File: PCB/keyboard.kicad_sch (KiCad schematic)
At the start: 118 parts, among them J101 USB4510-03-1-A, J103 CONN_DISPLAY, J2 AudioJack4, J4 switch, U2 USBLC6-2SC6, U3 USBLC6-2SC6, U4 RP2040, U5 W25Q128JVSIQ, Y1 12MHz

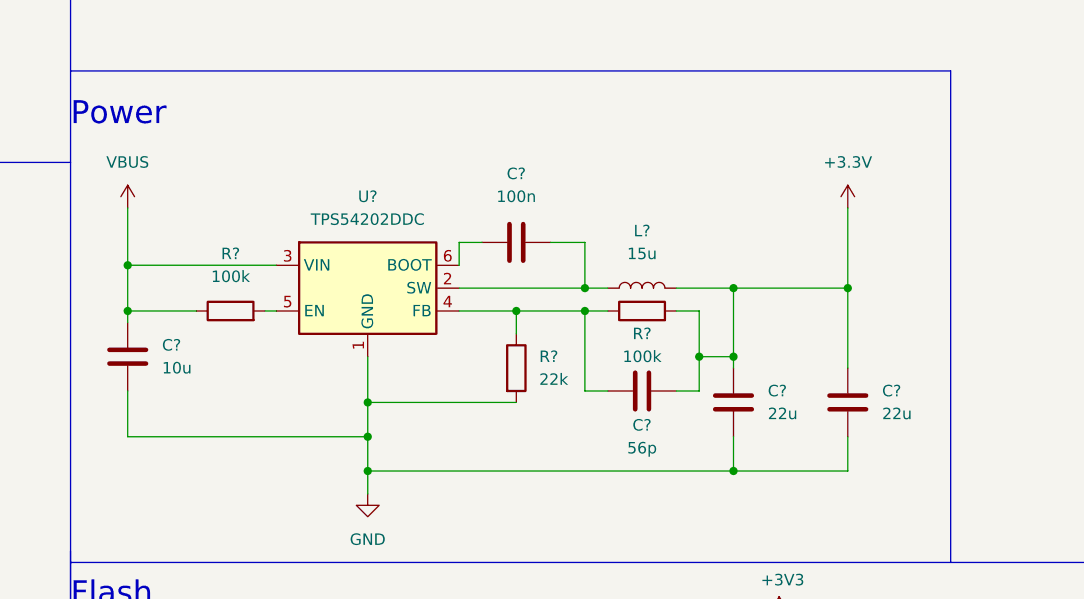
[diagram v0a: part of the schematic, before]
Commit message: Update footprint library
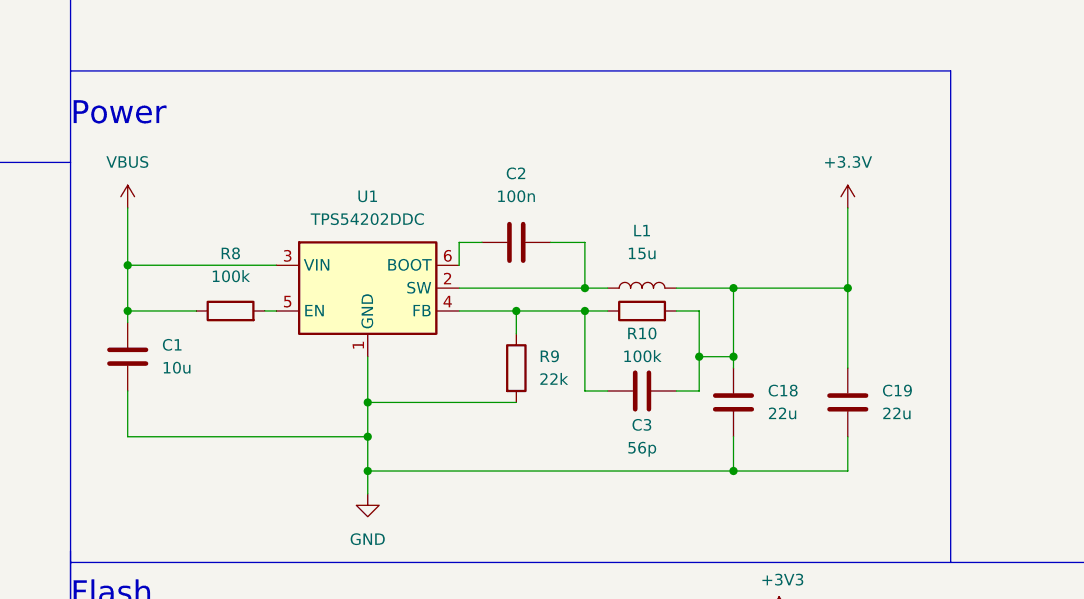
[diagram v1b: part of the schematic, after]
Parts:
- MX101, MX102, MX103, MX104, MX105, MX106, MX107, MX108, MX109, MX110, MX111, MX112, MX113, MX114, MX115, MX116, MX117, MX118, MX201, MX202, MX203, MX204, MX205, MX206, MX207, MX208, MX209, MX210, MX211, MX212, MX213, MX214, MX215, MX216, MX217, MX218: footprint SOFLE:CherryMX_KailhLowProfile_Hotswap -> Footprints:CherryMX_Choc_Hotswap
- gave numbers to parts that had none: 10

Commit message: wip full sch
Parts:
- removed U4: RP2040, RP2040:SC090813, symbol MCU_RaspberryPi_RP2040:RP2040
- added C201: 10u, symbol Device:C
- added C202: 100n, symbol Device:C
- added C203: 56p, symbol Device:C
- added C204, C205, C206, C207, C208, C209, C210, C211, C212, C215: 100n, Capacitor_SMD:C_0402_1005Metric, symbol Device:C
- added C213, C214: 1u, Capacitor_SMD:C_0402_1005Metric, symbol Device:C
- added C216, C217: 20p, Capacitor_SMD:C_0402_1005Metric, symbol Device:C
- added C218, C219: 22u, symbol Device:C
- added D221, D222: LED, symbol Device:LED
- added J201: USB4510-03-1-A, USB4510-03-1-A_GCT, symbol USB4510-03-1-A:USB4510-03-1-A
- added J202: AudioJack4, symbol Connector:AudioJack4
- added J203: CONN_DISPLAY, symbol Connector:Conn_01x04_Male
- added J204: switch, Connector_PinHeader_2.54mm:PinHeader_1x02_P2.54mm_Vertical, symbol Switch:SW_Push
- added L201: 15u, symbol Device:L
- added R201, R202: 5.1k, Resistor_SMD:R_0603_1608Metric, symbol Device:R
- added R203, R204: 27, Resistor_SMD:R_0402_1005Metric, symbol Device:R
- added R205: 10k, Resistor_SMD:R_0402_1005Metric, symbol Device:R
- added R206, R207: 1k, Resistor_SMD:R_0402_1005Metric, symbol Device:R
- added R208, R210: 100k, symbol Device:R
- added R209: 22k, symbol Device:R
- added R211, R212: 2.2K, Resistor_SMD:R_0402_1005Metric, symbol Device:R
- added R213, R214: 4.7K, Resistor_SMD:R_0402_1005Metric, symbol Device:R
- added U102, U103: USBLC6-2SC6, Package_TO_SOT_SMD:SOT-23-6, symbol Power_Protection:USBLC6-2SC6
- added U104, U204: RP2040, RP2040_minimal:RP2040-QFN-56, symbol Raspberry Pi:RP2040
- added U201: TPS54202DDC, Package_TO_SOT_SMD:SOT-23-6, symbol Regulator_Switching:TPS54202DDC
- added U205: W25Q128JVSIQ, Package_SO:SOIC-8_5.23x5.23mm_P1.27mm, symbol Memory_Flash:W25Q128JVS
- added Y201: 12MHz, Oscillator:Oscillator_SMD_Abracon_ASE-4Pin_3.2x2.5mm, symbol Device:Crystal_GND24
- J101: footprint USB4510-03-1-A:USB4510-03-1-A -> USB4510-03-1-A_GCT
- renumbered C1 to C101, C2 to C102, C3 to C103, C4 to C104, C5 to C105, C6 to C106, C7 to C107, C8 to C108, C9 to C109, C10 to C110, C11 to C111, C12 to C112, C13 to C113, C14 to C114, C15 to C115, C16 to C116, C17 to C117, C18 to C118, C19 to C119, DD103 to D103, D21 to D121, D22 to D122, J2 to J102, J4 to J104, L1 to L101, R1 to R101, R2 to R102, R3 to R103, R4 to R104, R5 to R105, R6 to R106, R7 to R107, R8 to R108, R9 to R109, R10 to R110, R13 to R111, R12 to R112, R108 to R113, R109 to R114, U1 to U101, U5 to U105, U2 to U202, U3 to U203, Y1 to Y101
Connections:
- net USB__CONN_D+ is gone; now on net USB_CONN_D+: J101.A6 (DP1), U202.1 (I/O1)
- net USB__CONN_D- is gone; now on net USB_CONN_D-: J101.A7 (DN1)
- net +1V1: now also C204.1, C205.1, C213.1, U104.23 (DVDD), U104.45 (VREG_VOUT), U104.50 (DVDD), U204.23 (DVDD), U204.45 (VREG_VOUT), U204.50 (DVDD)
- net +3.3V: now also C203.1, C218.1, C219.1, J203.2 (Pin_2), L201.2, R210.2, Y201.4
- net +3V3: now also C206.1, C207.1, C208.1, C209.1, C210.1, C211.1, C212.1, C214.1, C215.1, D222.2 (A), J202.S, R205.1, R213.2, R214.2, U103.5 (VBUS), U104.1 (IOVDD), U104.10 (IOVDD), U104.22 (IOVDD), U104.33 (IOVDD), U104.42 (IOVDD), U104.43 (ADC_AVDD), U104.44 (VREG_IN), U104.48 (USB_VDD), U104.49 (IOVDD), U204.1 (IOVDD), U204.10 (IOVDD), U204.22 (IOVDD), U204.33 (IOVDD), U204.42 (IOVDD), U204.43 (ADC_AVDD), U204.44 (VREG_IN), U204.48 (USB_VDD), U204.49 (IOVDD), U205.8 (VCC)
- net CC1: now also J201.A5 (CC1), R201.2
- net CC2: now also J201.B5 (CC2), R202.2
- net GND: now also J101.B4-A9 (VBUS), C201.2, C204.2, C205.2, C206.2, C207.2, C208.2, C209.2, C210.2, C211.2, C212.2, C213.2, C214.2, C215.2, C216.2, C217.2, C218.2, C219.2, J201.A1-B12 (GND), J201.B4-A9 (VBUS), J202.T, J203.1 (Pin_1), J204.2, R201.1, R202.1, R209.2, R211.1, R212.1, U102.2 (GND), U103.2 (GND), U104.19 (TESTEN), U104.57 (GND), U201.1 (GND), U204.19 (TESTEN), U204.57 (GND), U205.4 (GND), Y201.2; no longer J101.B1-A12 (GND)
- net GPIO26_ADC0: now also U204.38 (GPIO26_ADC0)
- net GPIO27_ADC1: now also U204.39 (GPIO27_ADC1)
- net GPIO28_ADC2: now also U204.40 (GPIO28_ADC2)
- net GPIO29_ADC3: now also U204.41 (GPIO29_ADC3)
- net L-COL-1: now also MX101.1, MX102.1, MX103.1, U104.7 (GPIO5); no longer MX201.1, MX202.1, MX203.1
- net L-COL-2: now also MX104.1, MX105.1, MX106.1, U104.8 (GPIO6); no longer MX204.1, MX205.1, MX206.1
- net L-COL-3: now also MX107.1, MX108.1, MX109.1, U104.9 (GPIO7); no longer MX207.1, MX208.1, MX209.1
- net L-COL-4: now also MX110.1, MX111.1, MX112.1, U104.11 (GPIO8); no longer MX210.1, MX211.1, MX212.1
- net L-COL-5: now also MX113.1, MX114.1, MX115.1, U104.12 (GPIO9); no longer MX213.1, MX214.1, MX215.1
- net L-COL-6: now also MX116.1, MX117.1, MX118.1, U104.13 (GPIO10); no longer MX216.1, MX217.1, MX218.1
- net L-ROW-1: now also D101.1 (K), D104.1 (K), D107.1 (K), D110.1 (K), D113.1 (K), D116.1 (K), U104.4 (GPIO2); no longer D201.1 (K), D204.1 (K), D207.1 (K), D210.1 (K), D213.1 (K), D216.1 (K)
- net L-ROW-2: now also D102.1 (K), D105.1 (K), D108.1 (K), D111.1 (K), D114.1 (K), D117.1 (K), U104.5 (GPIO3); no longer D202.1 (K), D205.1 (K), D208.1 (K), D211.1 (K), D214.1 (K), D217.1 (K)
- net L-ROW-3: now also D103.1 (K), D106.1 (K), D109.1 (K), D112.1 (K), D115.1 (K), D118.1 (K), U104.6 (GPIO4); no longer D203.1 (K), D206.1 (K), D209.1 (K), D212.1 (K), D215.1 (K), D218.1 (K)
- net LED: now also D221.2 (A), U204.37 (GPIO25); no longer D121.2 (A)
- net QSPI_SCLK: now also U204.52 (QSPI_SCLK), U205.6 (CLK)
- net QSPI_SD0: now also U204.53 (QSPI_SD0), U205.5 (DI(IO0))
- net QSPI_SD1: now also U204.55 (QSPI_SD1), U205.2 (DO(IO1))
- net QSPI_SD2: now also U204.54 (QSPI_SD2), U205.3 (IO2)
- net QSPI_SD3: now also U204.51 (QSPI_SD3), U205.7 (IO3)
- net QSPI_SS: now also R205.2, R206.1, U204.56 (QSPI_SS), U205.1 (~{CS})
- net R-COL-1: now also MX201.1, MX202.1, MX203.1, U204.7 (GPIO5); no longer MX101.1, MX102.1, MX103.1
- net R-COL-2: now also MX204.1, MX205.1, MX206.1, U204.8 (GPIO6); no longer MX104.1, MX105.1, MX106.1
- net R-COL-3: now also MX207.1, MX208.1, MX209.1, U204.9 (GPIO7); no longer MX107.1, MX108.1, MX109.1
- net R-COL-4: now also MX210.1, MX211.1, MX212.1, U204.11 (GPIO8); no longer MX110.1, MX111.1, MX112.1
- net R-COL-5: now also MX213.1, MX214.1, MX215.1, U204.12 (GPIO9); no longer MX113.1, MX114.1, MX115.1
- net R-COL-6: now also MX216.1, MX217.1, MX218.1, U204.13 (GPIO10); no longer MX116.1, MX117.1, MX118.1
- net R-ROW-1: now also D201.1 (K), D204.1 (K), D207.1 (K), D210.1 (K), D213.1 (K), D216.1 (K), U204.4 (GPIO2); no longer D101.1 (K), D104.1 (K), D107.1 (K), D110.1 (K), D113.1 (K), D116.1 (K)
- net R-ROW-2: now also D202.1 (K), D205.1 (K), D208.1 (K), D211.1 (K), D214.1 (K), D217.1 (K), U204.5 (GPIO3); no longer D102.1 (K), D105.1 (K), D108.1 (K), D111.1 (K), D114.1 (K), D117.1 (K)
- net R-ROW-3: now also D203.1 (K), D206.1 (K), D209.1 (K), D212.1 (K), D215.1 (K), D218.1 (K), U204.6 (GPIO4); no longer D103.1 (K), D106.1 (K), D109.1 (K), D112.1 (K), D115.1 (K), D118.1 (K)
- net RUN: now also U204.26 (RUN)
- net RX_SPLIT: now also U103.6 (I/O1), U204.3 (GPIO1)
- net RX_SPLIT_CONN: now also J202.R2, U103.1 (I/O1)
- net SCL_DISPLAY: now also J203.3 (Pin_3), R214.1, U204.18 (GPIO15)
- net SDA_DISPLAY: now also J203.4 (Pin_4), R213.1, U204.17 (GPIO14)
- net SWCLK: now also U204.24 (SWCLK)
- net SWD: now also U204.25 (SWD)
- net TX_SPLIT: now also U103.4 (I/O2), U204.2 (GPIO0)
- net TX_SPLIT_CONN: now also J202.R1, U103.3 (I/O2)
- net USB_CONN_D+: now also J201.A6 (DP1), J201.B6 (DP2), U102.1 (I/O1)
- net USB_CONN_D-: now also J201.A7 (DN1), J201.B7 (DN2), U102.3 (I/O2)
- net USB_D+: now also R203.1, U102.6 (I/O1)
- net USB_D-: now also R204.1, U102.4 (I/O2)
- net VBUS: now also J101.B1-A12 (GND), C201.1, J201.A4-B9 (VBUS), J201.B1-A12 (GND), R208.1, U102.5 (VBUS), U201.3 (VIN); no longer J101.B4-A9 (VBUS)
- net XIN: now also C216.1, U204.20 (XIN), Y201.1
- net XOUT: now also R207.1, U204.21 (XOUT)
- net at R104.2: now also U104.46 (USB_DM)
- net at R103.2: now also U104.47 (USB_DP)
- net ~{USB_BOOT} renamed ~{L_BOOT}
- new net: C202.1, U201.6 (BOOT)
- new net: C202.2, L201.1, U201.2 (SW)
- new net: C217.1, R207.2, Y201.3
- new net: R208.2, U201.5 (EN)
- new net: C203.2, R209.1, R210.1, U201.4 (FB)
- new net: D222.1 (K), R211.2
- new net: R204.2, U204.46 (USB_DM)
- new net: R203.2, U204.47 (USB_DP)
- new net: D221.1 (K), R212.2
- new net L_LED: D121.2 (A), U104.37 (GPIO25)
- new net L_QSPI_SCLK: U104.52 (QSPI_SCLK)
- new net L_QSPI_SD0: U104.53 (QSPI_SD0)
- new net L_QSPI_SD1: U104.55 (QSPI_SD1)
- new net L_QSPI_SD2: U104.54 (QSPI_SD2)
- new net L_QSPI_SD3: U104.51 (QSPI_SD3)
- new net L_QSPI_SS: U104.56 (QSPI_SS)
- new net L_RUN: U104.26 (RUN)
- new net L_RX_SPLIT: U104.3 (GPIO1)
- new net L_SCL_DISPLAY: U104.18 (GPIO15)
- new net L_SDA_DISPLAY: U104.17 (GPIO14)
- new net L_SWCLK: U104.24 (SWCLK)
- new net L_SWD: U104.25 (SWD)
- new net L_TX_SPLIT: U104.2 (GPIO0)
- new net L_XIN: U104.20 (XIN)
- new net L_XOUT: U104.21 (XOUT)
- new net ~{R_BOOT}: J204.1, R206.2
- no-connect marks 14 -> 32
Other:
- added sheet USB Input (usb_input.kicad_sch)
- note added: "Left Flash"
- note added: "Left MCU"
- note added: "Left Power"
- note added: "Right Flash"
- note added: "Right MCU"
- note added: "Right Matrix"
- note added: "Right Power"
- note removed: "Flash"
- note removed: "MCU"
- note removed: "Power"
- note removed: "Right matrix"
- moved on the sheet: C101, C102, C103, C104, C105, C106, C107, C108, C109, C110, C111, C112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

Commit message: Layout done
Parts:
- removed C101, C201: 10u, symbol Device:C
- removed C102, C202: 100n, symbol Device:C
- removed C103, C203: 56p, symbol Device:C
- removed C104, C105, C106, C107, C108, C109, C110, C111, C112, C115, C204, C205, C206, C207, C208, C209, C210, C211, C212, C215: 100n, Capacitor_SMD:C_0402_1005Metric, symbol Device:C
- removed C113, C114, C213, C214: 1u, Capacitor_SMD:C_0402_1005Metric, symbol Device:C
- removed C116, C117, C216, C217: 20p, Capacitor_SMD:C_0402_1005Metric, symbol Device:C
- removed C118, C119, C218, C219: 22u, symbol Device:C
- removed D101, D102, D103, D104, D105, D106, D107, D108, D109, D110, D111, D112, D113, D114, D115, D116, D117, D118, D201, D202, D203, D204, D205, D206, D207, D208, D209, D210, D211, D212, D213, D214, D215, D216, D217, D218: DIODE, Diode_SMD:D_SOD-123, symbol Diode:1N4148W
- removed D121, D122, D221, D222: LED, symbol Device:LED
- removed J101, J201: USB4510-03-1-A, USB4510-03-1-A_GCT, symbol USB4510-03-1-A:USB4510-03-1-A
- removed J102, J202: AudioJack4, symbol Connector:AudioJack4
- removed J103, J203: CONN_DISPLAY, symbol Connector:Conn_01x04_Male
- removed J104, J204: switch, Connector_PinHeader_2.54mm:PinHeader_1x02_P2.54mm_Vertical, symbol Switch:SW_Push
- removed L101, L201: 15u, symbol Device:L
- removed MX101, MX102, MX103, MX104, MX105, MX106, MX107, MX108, MX109, MX110, MX111, MX112, MX113, MX114, MX115, MX116, MX117, MX118, MX201, MX202, MX203, MX204, MX205, MX206, MX207, MX208, MX209, MX210, MX211, MX212, MX213, MX214, MX215, MX216, MX217, MX218: SW_Push, Footprints:CherryMX_Choc_Hotswap, symbol Switch:SW_Push
- removed R101, R102, R201, R202: 5.1k, Resistor_SMD:R_0603_1608Metric, symbol Device:R
- removed R103, R104, R203, R204: 27, Resistor_SMD:R_0402_1005Metric, symbol Device:R
- removed R105, R205: 10k, Resistor_SMD:R_0402_1005Metric, symbol Device:R
- removed R106, R107, R206, R207: 1k, Resistor_SMD:R_0402_1005Metric, symbol Device:R
- removed R108, R110, R208, R210: 100k, symbol Device:R
- removed R109, R209: 22k, symbol Device:R
- removed R111, R112, R211, R212: 2.2K, Resistor_SMD:R_0402_1005Metric, symbol Device:R
- removed R113, R114, R213, R214: 4.7K, Resistor_SMD:R_0402_1005Metric, symbol Device:R
- removed U101, U201: TPS54202DDC, Package_TO_SOT_SMD:SOT-23-6, symbol Regulator_Switching:TPS54202DDC
- removed U102, U103, U202, U203: USBLC6-2SC6, Package_TO_SOT_SMD:SOT-23-6, symbol Power_Protection:USBLC6-2SC6
- removed U104, U204: RP2040, RP2040_minimal:RP2040-QFN-56, symbol Raspberry Pi:RP2040
- removed U105, U205: W25Q128JVSIQ, Package_SO:SOIC-8_5.23x5.23mm_P1.27mm, symbol Memory_Flash:W25Q128JVS
- removed Y101, Y201: 12MHz, Oscillator:Oscillator_SMD_Abracon_ASE-4Pin_3.2x2.5mm, symbol Device:Crystal_GND24
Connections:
- no-connect marks 32 -> 0
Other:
- removed sheet USB Input
- added sheet Left MCU (mcu.kicad_sch)
- added sheet Left Matix (key_matrix.kicad_sch)
- added sheet Right MCU (mcu.kicad_sch)
- added sheet Right Matrix (key_matrix.kicad_sch)
- added sheet TRRS Connection (trrs_conn.kicad_sch)
- note removed: "Connectors"
- note removed: "Crystal"
- note removed: "ESD Protection"
- note removed: "LEDs"
- note removed: "Left Flash"
- note removed: "Left MCU"
- note removed: "Left Matrix"
- note removed: "Left Power"
- note removed: "Make sure C13 is close to pin 45 of RP2040"
- note removed: "Make sure C14 is close to pin 44 of RP2040"
- note removed: "Make sure R3 and R4 are close to RP2040"
- note removed: "Make sure U2 is close to J1"
- note removed: "Right Flash"
- note removed: "Right MCU"
- note removed: "Right Matrix"
- note removed: "Right Power"
- note removed: "Route right half TX to left half RX Route left half TX to right half RX"
- note removed: "Thumb keys"
- title: (none) -> 36

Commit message: Work
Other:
- sheet Left MCU ports: added ROW-4; removed COL-6
- sheet Left Matix ports: added ROW-4; removed COL-6
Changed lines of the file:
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@@
     (rev "1.0")
   )
+  (wire (pts (xy 68.58 62.23) (xy 72.39 62.23))
+    (stroke (width 0) (type default) (color 0 0 0 0))
+  )
+  (wire (pts (xy 133.35 48.26) (xy 137.16 48.26))
+    (stroke (width 0) (type default) (color 0 0 0 0))
+  )
+  (wire (pts (xy 133.35 53.34) (xy 137.16 53.34))
+    (stroke (width 0) (type default) (color 0 0 0 0))
+  )
+  (wire (pts (xy 133.35 50.8) (xy 137.16 50.8))
+    (stroke (width 0) (type default) (color 0 0 0 0))
+  )
+  (wire (pts (xy 133.35 58.42) (xy 137.16 58.42))
+    (stroke (width 0) (type default) (color 0 0 0 0))
+  )
+  (wire (pts (xy 133.35 64.77) (xy 137.16 64.77))
+    (stroke (width 0) (type default) (color 0 0 0 0))
+  )
+  (wire (pts (xy 68.58 55.88) (xy 72.39 55.88))
+    (stroke (width 0) (type default) (color 0 0 0 0))
+  )
+  (wire (pts (xy 133.35 69.85) (xy 137.16 69.85))
+    (stroke (width 0) (type default) (color 0 0 0 0))
+  )
+  (wire (pts (xy 92.71 72.39) (xy 95.25 72.39))
+    (stroke (width 0) (type default) (color 0 0 0 0))
+  )
+  (wire (pts (xy 133.35 67.31) (xy 137.16 67.31))
+    (stroke (width 0) (type default) (color 0 0 0 0))
+  )
+  (wire (pts (xy 68.58 69.85) (xy 72.39 69.85))
+    (stroke (width 0) (type default) (color 0 0 0 0))
+  )
+  (wire (pts (xy 133.35 55.88) (xy 137.16 55.88))
+    (stroke (width 0) (type default) (color 0 0 0 0))
+  )
+  (wire (pts (xy 92.71 69.85) (xy 95.25 69.85))
+    (stroke (width 0) (type default) (color 0 0 0 0))
+  )
+  (wire (pts (xy 68.58 67.31) (xy 72.39 67.31))
+    (stroke (width 0) (type default) (color 0 0 0 0))
+  )
+  (wire (pts (xy 133.35 60.96) (xy 137.16 60.96))
+    (stroke (width 0) (type default) (color 0 0 0 0))
+  )
+  (wire (pts (xy 111.76 72.39) (xy 114.3 72.39))
+    (stroke (width 0) (type default) (color 0 0 0 0))
+  )
+  (polyline (pts (xy 299.72 165.1) (xy 299.72 165.1))
+    (stroke (width 0) (type default) (color 0 0 0 0))
+  )
+  (wire (pts (xy 68.58 53.34) (xy 72.39 53.34))
+    (stroke (width 0) (type default) (color 0 0 0 0))
+  )
+  (wire (pts (xy 68.58 48.26) (xy 72.39 48.26))
+    (stroke (width 0) (type default) (color 0 0 0 0))
+  )
+  (wire (pts (xy 111.76 69.85) (xy 114.3 69.85))
+    (stroke (width 0) (type default) (color 0 0 0 0))
+  )
+  (wire (pts (xy 68.58 50.8) (xy 72.39 50.8))
+    (stroke (width 0) (type default) (color 0 0 0 0))
+  )
   (wire (pts (xy 68.58 64.77) (xy 72.39 64.77))
     (stroke (width 0) (type default) (color 0 0 0 0))
   )
-  (wire (pts (xy 133.35 48.26) (xy 137.16 48.26))
-    (stroke (width 0) (type default) (color 0 0 0 0))
-  )
-  (wire (pts (xy 133.35 53.34) (xy 137.16 53.34))
-    (stroke (width 0) (type default) (color 0 0 0 0))
-  )
-  (wire (pts (xy 133.35 50.8) (xy 137.16 50.8))
-    (stroke (width 0) (type default) (color 0 0 0 0))
-  )
-  (wire (pts (xy 133.35 58.42) (xy 137.16 58.42))
-    (stroke (width 0) (type default) (color 0 0 0 0))
-  )
-  (wire (pts (xy 133.35 64.77) (xy 137.16 64.77))
-    (stroke (width 0) (type default) (color 0 0 0 0))
-  )
-  (wire (pts (xy 68.58 55.88) (xy 72.39 55.88))
-    (stroke (width 0) (type default) (color 0 0 0 0))
-  )
-  (wire (pts (xy 133.35 69.85) (xy 137.16 69.85))
-    (stroke (width 0) (type default) (color 0 0 0 0))
-  )
-  (wire (pts (xy 92.71 72.39) (xy 95.25 72.39))
-    (stroke (width 0) (type default) (color 0 0 0 0))
-  )
-  (wire (pts (xy 133.35 67.31) (xy 137.16 67.31))
-    (stroke (width 0) (type default) (color 0 0 0 0))
-  )
-  (wire (pts (xy 133.35 55.88) (xy 137.16 55.88))
-    (stroke (width 0) (type default) (color 0 0 0 0))
-  )
-  (wire (pts (xy 92.71 69.85) (xy 95.25 69.85))
-    (stroke (width 0) (type default) (color 0 0 0 0))
-  )
-  (wire (pts (xy 68.58 69.85) (xy 72.39 69.85))
-    (stroke (width 0) (type default) (color 0 0 0 0))
-  )
-  (wire (pts (xy 68.58 60.96) (xy 72.39 60.96))
-    (stroke (width 0) (type default) (color 0 0 0 0))
-  )
-  (wire (pts (xy 133.35 60.96) (xy 137.16 60.96))
-    (stroke (width 0) (type default) (color 0 0 0 0))
-  )
-  (wire (pts (xy 111.76 72.39) (xy 114.3 72.39))
-    (stroke (width 0) (type default) (color 0 0 0 0))
-  )
-  (polyline (pts (xy 299.72 165.1) (xy 299.72 165.1))
-    (stroke (width 0) (type default) (color 0 0 0 0))
-  )
-  (wire (pts (xy 68.58 53.34) (xy 72.39 53.34))
-    (stroke (width 0) (type default) (color 0 0 0 0))
-  )
-  (wire (pts (xy 68.58 48.26) (xy 72.39 48.26))
-    (stroke (width 0) (type default) (color 0 0 0 0))
-  )
-  (wire (pts (xy 111.76 69.85) (xy 114.3 69.85))
-    (stroke (width 0) (type default) (color 0 0 0 0))
-  )
-  (wire (pts (xy 68.58 50.8) (xy 72.39 50.8))
-    (stroke (width 0) (type default) (color 0 0 0 0))
-  )
-  (wire (pts (xy 68.58 67.31) (xy 72.39 67.31))
-    (stroke (width 0) (type default) (color 0 0 0 0))
-  )
   (wire (pts (xy 68.58 58.42) (xy 72.39 58.42))
     (stroke (width 0) (type default) (color 0 0 0 0))
@@
       (effects (font (size 1.27 1.27)) (justify left top) hide)
     )
-    (pin "ROW-2" input (at 68.58 67.31 0)
-      (effects (font (size 1.27 1.27)) (justify right))
-    )
-    (pin "ROW-3" input (at 68.58 69.85 0)
-      (effects (font (size 1.27 1.27)) (justify right))
-    )
-    (pin "ROW-1" input (at 68.58 64.77 0)
+    (pin "ROW-2" input (at 68.58 64.77 0)
+      (effects (font (size 1.27 1.27)) (justify right))
+    )
+    (pin "ROW-3" input (at 68.58 67.31 0)
+      (effects (font (size 1.27 1.27)) (justify right))
+    )
+    (pin "ROW-1" input (at 68.58 62.23 0)
       (effects (font (size 1.27 1.27)) (justify right))
     )
@@
       (effects (font (size 1.27 1.27)) (justify right))
     )
-    (pin "COL-6" input (at 68.58 60.96 0)
+    (pin "ROW-4" input (at 68.58 69.85 0)
       (effects (font (size 1.27 1.27)) (justify right))
     )
@@
       (effects (font (size 1.27 1.27)) (justify left top) hide)
     )
-    (pin "COL-6" input (at 72.39 60.96 180)
-      (effects (font (size 1.27 1.27)) (justify left))
-    )
     (pin "COL-3" input (at 72.39 53.34 180)
       (effects (font (size 1.27 1.27)) (justify left))
@@
       (effects (font (size 1.27 1.27)) (justify left))
     )
-    (pin "ROW-2" input (at 72.39 67.31 180)
-      (effects (font (size 1.27 1.27)) (justify left))
-    )
-    (pin "ROW-3" input (at 72.39 69.85 180)
-      (effects (font (size 1.27 1.27)) (justify left))
-    )
-    (pin "ROW-1" input (at 72.39 64.77 180)
+    (pin "ROW-2" input (at 72.39 64.77 180)
+      (effects (font (size 1.27 1.27)) (justify left))
+    )
+    (pin "ROW-3" input (at 72.39 67.31 180)
+      (effects (font (size 1.27 1.27)) (justify left))
+    )
+    (pin "ROW-1" input (at 72.39 62.23 180)
       (effects (font (size 1.27 1.27)) (justify left))
     )
@@
       (effects (font (size 1.27 1.27)) (justify right))
     )
-  )
+    (pin "ROW-4" input (at 72.39 69.85 180)
+      (effects (font (size 1.27 1.27)) (justify left))
+    )
+  )
